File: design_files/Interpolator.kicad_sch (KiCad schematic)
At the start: 74 parts, among them J1 DA15_Receptacle_MountingHoles, J2 DA15_Receptacle_MountingHoles, J3 Conn_01x12, J4 Conn_01x12, SW1 SW_Push, U1 UA9638C, U2 UA9638C, U3 ICTW8, U5 24AA02-OT, U6 MCP1754S-3302xMB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

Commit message: Add a readme and license
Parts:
- X1: footprint encoder-interpolator:Oscillator_SMD_EuroQuartz_XO91-4Pin_7.0x5.0mm -> encoder-interpolator:Oscillator5x3.2mm
- renumbered R20 to R19, R22 to R20
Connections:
- net +3.3V: now also RN4.5 (R4.2), RN4.6 (R3.2); no longer D1.2 (A), D2.2 (A)
- net FAULT: now also D1.1 (K); no longer RN4.3 (R3.1)
- net GND: now also RN4.7 (R2.2); no longer RN4.2 (R2.1)
- net STATUS: now also D2.1 (K); no longer RN4.4 (R4.1)
- net at D3.1 (K): now also RN4.2 (R2.1); no longer RN4.7 (R2.2)
- new net: D1.2 (A), RN4.3 (R3.1)
- new net: D2.2 (A), RN4.4 (R4.1)
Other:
- moved on the sheet: D1, D2, D3, D5, RN4

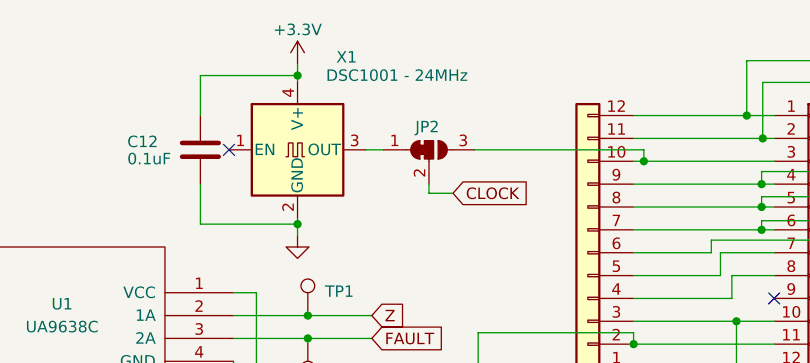
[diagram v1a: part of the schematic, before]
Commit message: Add a BOM and fab notes
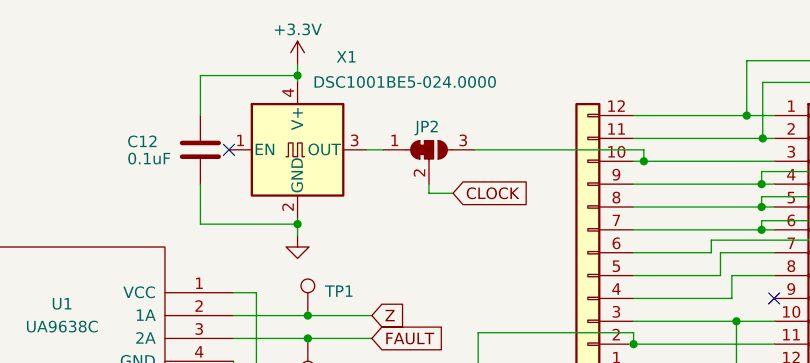
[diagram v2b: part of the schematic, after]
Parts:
- X1: value DSC1001 - 24MHz -> DSC1001BE5-024.0000
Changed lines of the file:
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@@
       (effects (font (size 1.27 1.27)))
     )
-    (property "Value" "DSC1001 - 24MHz" (at 115.316 20.32 0)
+    (property "Value" "DSC1001BE5-024.0000" (at 116.205 21.082 0)
       (effects (font (size 1.27 1.27)))
     )

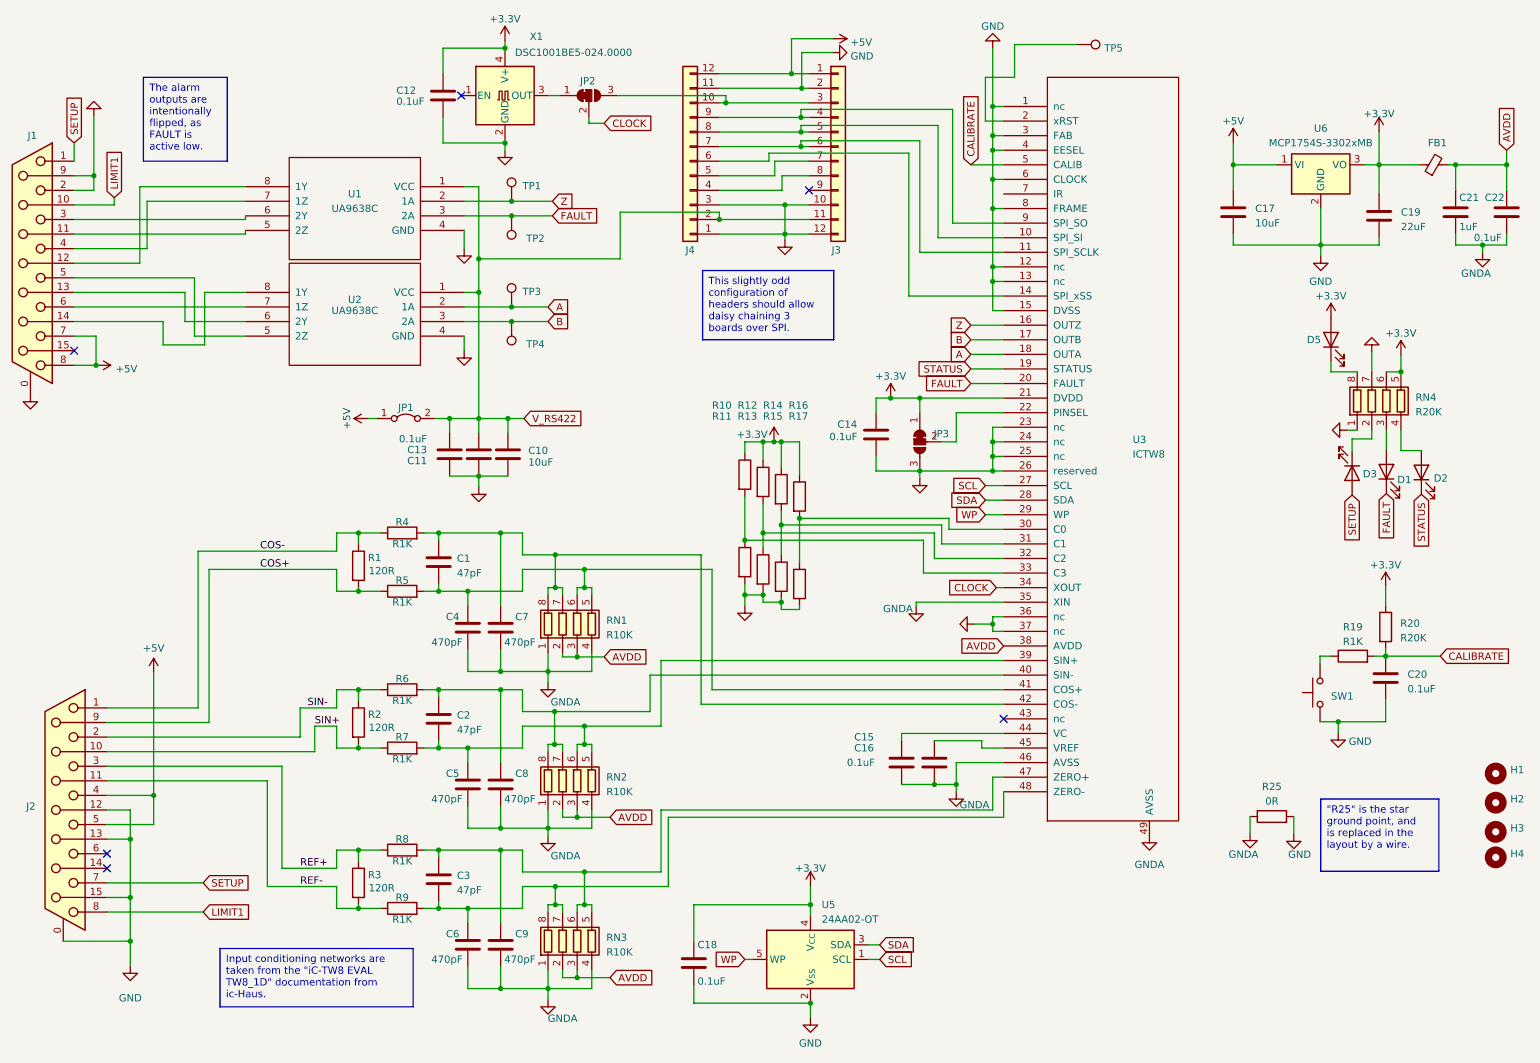
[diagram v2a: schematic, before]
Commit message: Revision 2, and update kicad version
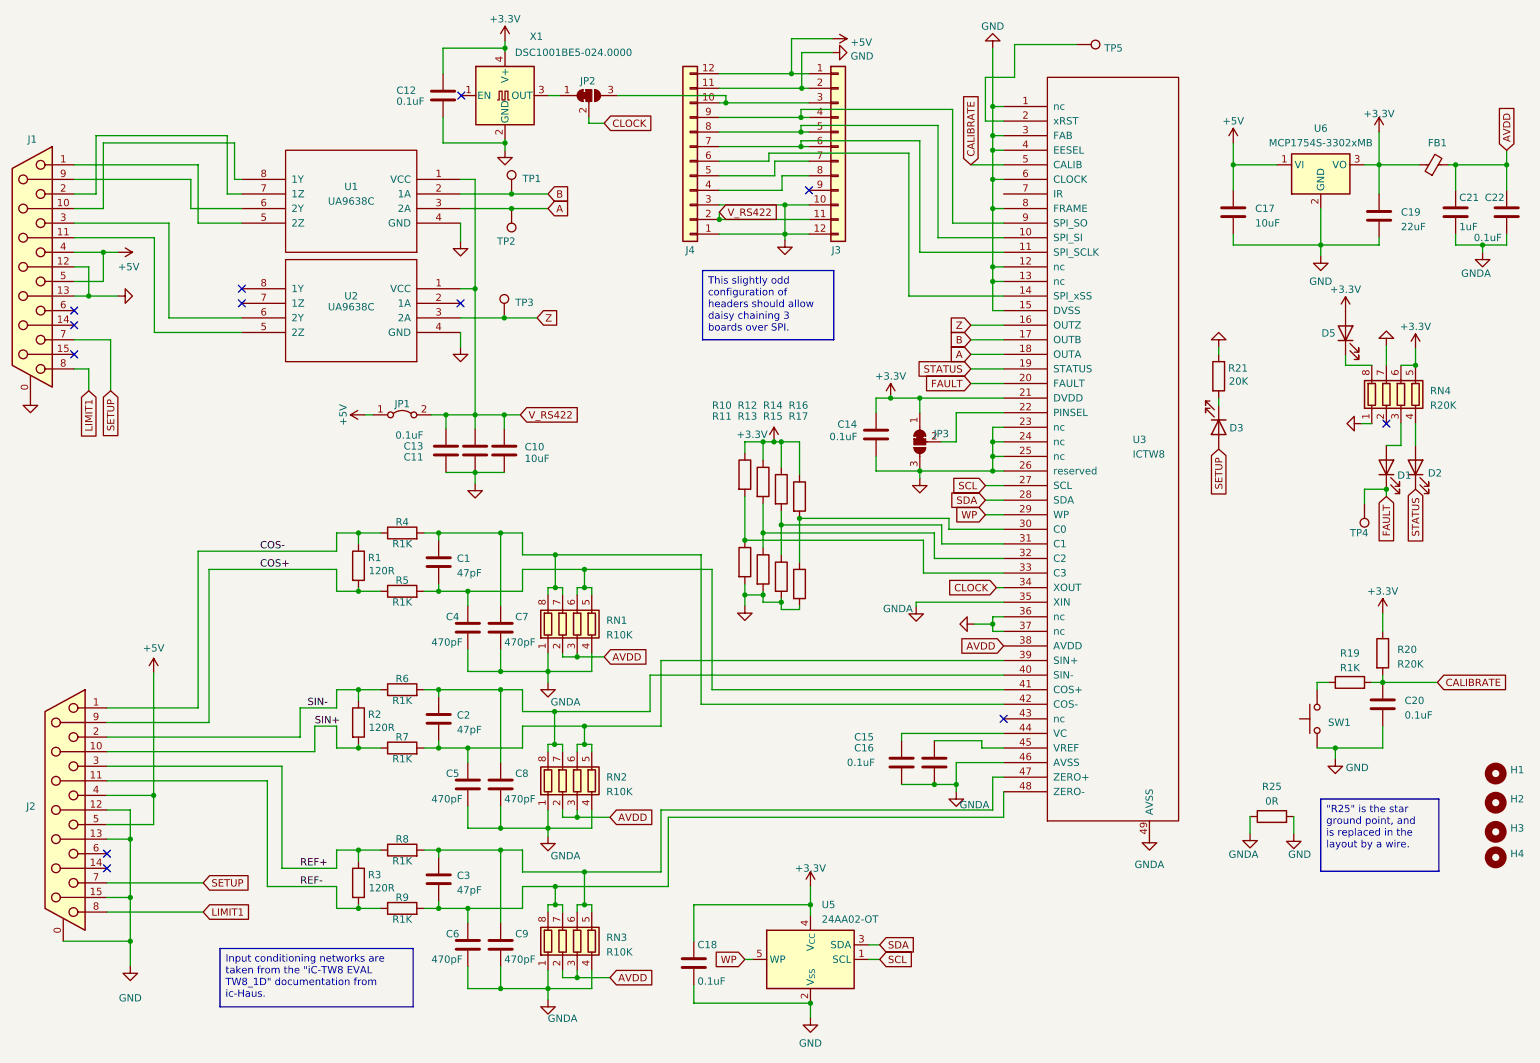
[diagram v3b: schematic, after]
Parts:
- added R21: 20K, encoder-interpolator:R_0603_1608Metric, symbol encoder-interpolator:R
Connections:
- net +5V: now also J1.4, J1.5; no longer J1.7, J1.8
- net A: now also TP2.1, U1.3 (2A); no longer TP3.1, U2.2 (1A)
- net B: now also TP1.1, U1.2 (1A); no longer TP4.1, U2.3 (2A)
- net FAULT: now also TP4.1; no longer TP2.1, U1.3 (2A)
- net GND: now also J1.12 (P12), J1.13 (P13), R21.1; no longer J1.2, J1.9 (P9)
- net LIMIT1: now also J1.8; no longer J1.10 (P10)
- net SETUP: now also J1.7; no longer J1.1
- net Z: now also TP3.1, U2.3 (2A); no longer TP1.1, U1.2 (1A)
- net at U2.5 (2Z): now also J1.11 (P111); no longer J1.5
- net at U2.6 (2Y): now also J1.3; no longer J1.13 (P13)
- net at U2.7 (1Z): no longer J1.6
- net at U2.8 (1Y): no longer J1.14 (P14)
- net at U1.5 (2Z): now also J1.1; no longer J1.11 (P111)
- net at U1.8 (1Y): now also J1.10 (P10); no longer J1.12 (P12)
- net at U1.6 (2Y): now also J1.9 (P9); no longer J1.3
- net at U1.7 (1Z): now also J1.2; no longer J1.4
- net at D3.1 (K): now also R21.2; no longer RN4.2 (R2.1)
- no-connect marks 6 -> 12
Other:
- moved on the sheet: C10, C11, C13, C20, D1, D2, D3, D5, J1, JP1, R19, R20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

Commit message: Pulldown the unused line driver input
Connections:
- net GND: now also U2.2 (1A)
- no-connect marks 12 -> 11
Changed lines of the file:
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@@
+	)
+	(junction
+		(at 96.52 69.85)
+		(diameter 0)
+		(color 0 0 0 0)
 	)
 	(junction
@@
 	)
 	(no_connect
-		(at 96.52 64.77)
-	)
-	(no_connect
 		(at 257.81 85.725)
 	)
@@
 	(wire
 		(pts
+			(xy 97.79 64.77) (xy 97.79 69.85)
+		)
+		(stroke
+			(width 0)
+			(type default)
+		)
+	)
+	(wire
+		(pts
 			(xy 78.74 114.935) (xy 74.93 114.935)
 		)
@@
 	(wire
 		(pts
+			(xy 96.52 69.85) (xy 97.79 69.85)
+		)
+		(stroke
+			(width 0)
+			(type default)
+		)
+	)
+	(wire
+		(pts
 			(xy 116.84 154.305) (xy 114.3 154.305)
 		)
@@
 		)
 		(stroke
+			(width 0)
+			(type default)
+		)
+	)
+	(wire
+		(pts
+			(xy 96.52 64.77) (xy 97.79 64.77)
+		)
+		(stroke
